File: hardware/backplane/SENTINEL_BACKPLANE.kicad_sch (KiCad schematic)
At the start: 57 parts, among them J1 SLOT1, J10 50V IN, J11 DRAIN1, J12 DRAIN2, J13 DRAIN3, J14 DRAIN4, J15 DRAIN5, J16 DRAIN6, J17 DRAIN7, J18 DRAIN8, J19 12V IN, J2 SLOT2, J3 SLOT3, J4 SLOT4, J5 SLOT5, J6 SLOT6, J7 SLOT7, J8 SLOT8, J9 TO TILE

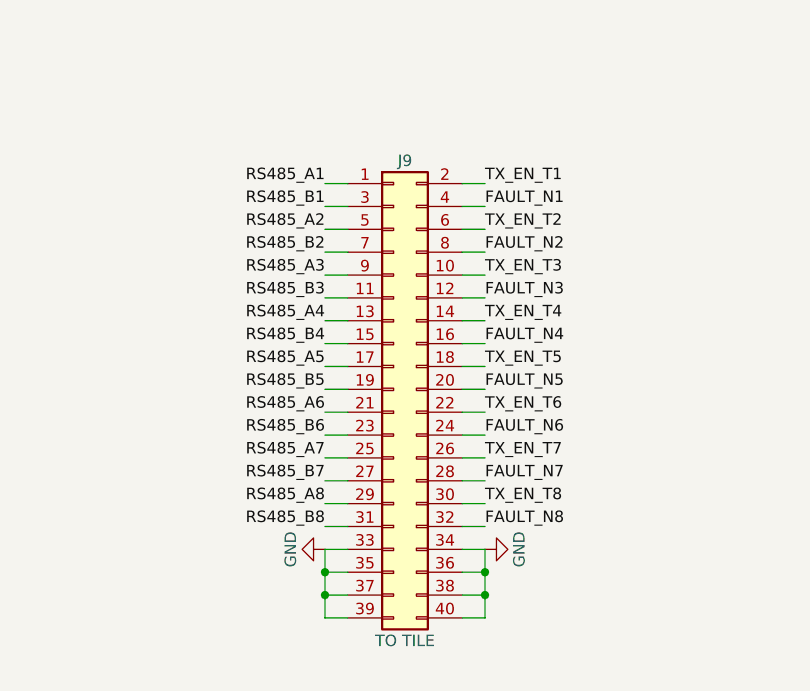
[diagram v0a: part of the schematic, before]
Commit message: Five boards DRC-clean, BOMs, layout engine improvements
- Backplane, clock & timing, calibration network, PSU and feed board layouts now pass
  KiCad DRC with zero errors and zero unconnected items
- T/R module: 0 DRC errors, 6 connections left to route by hand
- Calibration selector redesigned as an SPDT tree (replaces the fine-pitch SP8T)
- PSU: IPC-2221 2.5 mm high-voltage clearance via KiCad custom rules
- Backplane/tile cable re-pinned (slots 1-4 left column, 5-8 right) for routability
- Grouped BOM CSV for every board (hardware/tools/export_bom.sh)
- Router: partial routing, neck-downs at fine-pitch pins, long-axis fan-out,
  NPTH obstacles, pour-net connectivity, domain-aware clearance, rip-up tuning

Co-Authored-By: Claude Opus 5.5 <noreply@anthropic.com>
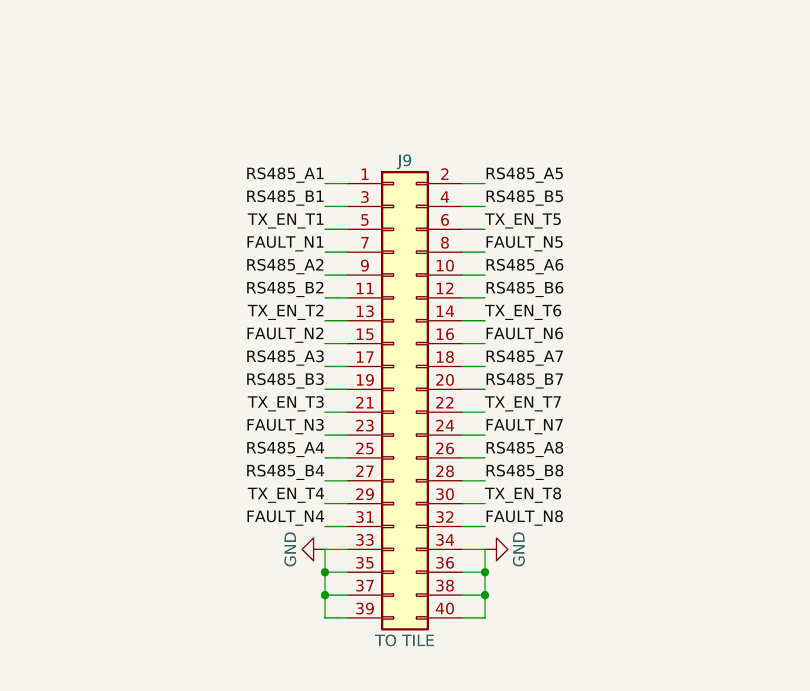
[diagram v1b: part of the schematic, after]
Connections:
- net FAULT_N1: now also J9.7 (Pin_7); no longer J9.4 (Pin_4)
- net FAULT_N2: now also J9.15 (Pin_15); no longer J9.8 (Pin_8)
- net FAULT_N3: now also J9.23 (Pin_23); no longer J9.12 (Pin_12)
- net FAULT_N4: now also J9.31 (Pin_31); no longer J9.16 (Pin_16)
- net FAULT_N5: now also J9.8 (Pin_8); no longer J9.20 (Pin_20)
- net FAULT_N6: now also J9.16 (Pin_16); no longer J9.24 (Pin_24)
- net FAULT_N7: now also J9.24 (Pin_24); no longer J9.28 (Pin_28)
- net RS485_A2: now also J9.9 (Pin_9); no longer J9.5 (Pin_5)
- net RS485_A3: now also J9.17 (Pin_17); no longer J9.9 (Pin_9)
- net RS485_A4: now also J9.25 (Pin_25); no longer J9.13 (Pin_13)
- net RS485_A5: now also J9.2 (Pin_2); no longer J9.17 (Pin_17)
- net RS485_A6: now also J9.10 (Pin_10); no longer J9.21 (Pin_21)
- net RS485_A7: now also J9.18 (Pin_18); no longer J9.25 (Pin_25)
- net RS485_A8: now also J9.26 (Pin_26); no longer J9.29 (Pin_29)
- net RS485_B2: now also J9.11 (Pin_11); no longer J9.7 (Pin_7)
- net RS485_B3: now also J9.19 (Pin_19); no longer J9.11 (Pin_11)
- net RS485_B4: now also J9.27 (Pin_27); no longer J9.15 (Pin_15)
- net RS485_B5: now also J9.4 (Pin_4); no longer J9.19 (Pin_19)
- net RS485_B6: now also J9.12 (Pin_12); no longer J9.23 (Pin_23)
- net RS485_B7: now also J9.20 (Pin_20); no longer J9.27 (Pin_27)
- net RS485_B8: now also J9.28 (Pin_28); no longer J9.31 (Pin_31)
- net TX_EN_T1: now also J9.5 (Pin_5); no longer J9.2 (Pin_2)
- net TX_EN_T2: now also J9.13 (Pin_13); no longer J9.6 (Pin_6)
- net TX_EN_T3: now also J9.21 (Pin_21); no longer J9.10 (Pin_10)
- net TX_EN_T4: now also J9.29 (Pin_29); no longer J9.14 (Pin_14)
- net TX_EN_T5: now also J9.6 (Pin_6); no longer J9.18 (Pin_18)
- net TX_EN_T6: now also J9.14 (Pin_14); no longer J9.22 (Pin_22)
- net TX_EN_T7: now also J9.22 (Pin_22); no longer J9.26 (Pin_26)
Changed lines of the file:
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@@
 		)
 	)
-	(label "TX_EN_T1"
+	(label "RS485_A5"
 		(at 289.56 193.04 0)
 		(fields_autoplaced yes)
@@
 		)
 	)
+	(label "RS485_B5"
+		(at 289.56 195.58 0)
+		(fields_autoplaced yes)
+		(effects
+			(font
+				(size 1.27 1.27)
+			)
+			(justify left bottom)
+		)
+	)
+	(label "TX_EN_T1"
+		(at 271.78 198.12 180)
+		(fields_autoplaced yes)
+		(effects
+			(font
+				(size 1.27 1.27)
+			)
+			(justify right bottom)
+		)
+	)
+	(label "TX_EN_T5"
+		(at 289.56 198.12 0)
+		(fields_autoplaced yes)
+		(effects
+			(font
+				(size 1.27 1.27)
+			)
+			(justify left bottom)
+		)
+	)
 	(label "FAULT_N1"
-		(at 289.56 195.58 0)
+		(at 271.78 200.66 180)
+		(fields_autoplaced yes)
+		(effects
+			(font
+				(size 1.27 1.27)
+			)
+			(justify right bottom)
+		)
+	)
+	(label "FAULT_N5"
+		(at 289.56 200.66 0)
 		(fields_autoplaced yes)
 		(effects
@@
 	)
 	(label "RS485_A2"
-		(at 271.78 198.12 180)
-		(fields_autoplaced yes)
-		(effects
-			(font
-				(size 1.27 1.27)
-			)
-			(justify right bottom)
+		(at 271.78 203.2 180)
+		(fields_autoplaced yes)
+		(effects
+			(font
+				(size 1.27 1.27)
+			)
+			(justify right bottom)
+		)
+	)
+	(label "RS485_A6"
+		(at 289.56 203.2 0)
+		(fields_autoplaced yes)
+		(effects
+			(font
+				(size 1.27 1.27)
+			)
+			(justify left bottom)
+		)
+	)
+	(label "RS485_B2"
+		(at 271.78 205.74 180)
+		(fields_autoplaced yes)
+		(effects
+			(font
+				(size 1.27 1.27)
+			)
+			(justify right bottom)
+		)
+	)
+	(label "RS485_B6"
+		(at 289.56 205.74 0)
+		(fields_autoplaced yes)
+		(effects
+			(font
+				(size 1.27 1.27)
+			)
+			(justify left bottom)
 		)
 	)
 	(label "TX_EN_T2"
-		(at 289.56 198.12 0)
-		(fields_autoplaced yes)
-		(effects
-			(font
-				(size 1.27 1.27)
-			)
-			(justify left bottom)
-		)
-	)
-	(label "RS485_B2"
-		(at 271.78 200.66 180)
-		(fields_autoplaced yes)
-		(effects
-			(font
-				(size 1.27 1.27)
-			)
-			(justify right bottom)
+		(at 271.78 208.28 180)
+		(fields_autoplaced yes)
+		(effects
+			(font
+				(size 1.27 1.27)
+			)
+			(justify right bottom)
+		)
+	)
+	(label "TX_EN_T6"
+		(at 289.56 208.28 0)
+		(fields_autoplaced yes)
+		(effects
+			(font
+				(size 1.27 1.27)
+			)
+			(justify left bottom)
 		)
 	)
 	(label "FAULT_N2"
-		(at 289.56 200.66 0)
+		(at 271.78 210.82 180)
+		(fields_autoplaced yes)
+		(effects
+			(font
+				(size 1.27 1.27)
+			)
+			(justify right bottom)
+		)
+	)
+	(label "FAULT_N6"
+		(at 289.56 210.82 0)
 		(fields_autoplaced yes)
 		(effects
@@
 	)
 	(label "RS485_A3"
-		(at 271.78 203.2 180)
-		(fields_autoplaced yes)
-		(effects
-			(font
-				(size 1.27 1.27)
-			)
-			(justify right bottom)
+		(at 271.78 213.36 180)
+		(fields_autoplaced yes)
+		(effects
+			(font
+				(size 1.27 1.27)
+			)
+			(justify right bottom)
+		)
+	)
+	(label "RS485_A7"
+		(at 289.56 213.36 0)
+		(fields_autoplaced yes)
+		(effects
+			(font
+				(size 1.27 1.27)
+			)
+			(justify left bottom)
+		)
+	)
+	(label "RS485_B3"
+		(at 271.78 215.9 180)
+		(fields_autoplaced yes)
+		(effects
+			(font
+				(size 1.27 1.27)
+			)
+			(justify right bottom)
+		)
+	)
+	(label "RS485_B7"
+		(at 289.56 215.9 0)
+		(fields_autoplaced yes)
+		(effects
+			(font
+				(size 1.27 1.27)
+			)
+			(justify left bottom)
 		)
 	)
 	(label "TX_EN_T3"
-		(at 289.56 203.2 0)
-		(fields_autoplaced yes)
-		(effects
-			(font
-				(size 1.27 1.27)
-			)
-			(justify left bottom)
-		)
-	)
-	(label "RS485_B3"
-		(at 271.78 205.74 180)
-		(fields_autoplaced yes)
-		(effects
-			(font
-				(size 1.27 1.27)
-			)
-			(justify right bottom)
+		(at 271.78 218.44 180)
+		(fields_autoplaced yes)
+		(effects
+			(font
+				(size 1.27 1.27)
+			)
+			(justify right bottom)
+		)
+	)
+	(label "TX_EN_T7"
+		(at 289.56 218.44 0)
+		(fields_autoplaced yes)
+		(effects
+			(font
+				(size 1.27 1.27)
+			)
+			(justify left bottom)
 		)
 	)
 	(label "FAULT_N3"
-		(at 289.56 205.74 0)
+		(at 271.78 220.98 180)
+		(fields_autoplaced yes)
+		(effects
+			(font
+				(size 1.27 1.27)
+			)
+			(justify right bottom)
+		)
+	)
+	(label "FAULT_N7"
+		(at 289.56 220.98 0)
 		(fields_autoplaced yes)
 		(effects
@@
 	)
 	(label "RS485_A4"
-		(at 271.78 208.28 180)
-		(fields_autoplaced yes)
-		(effects
-			(font
-				(size 1.27 1.27)
-			)
-			(justify right bottom)
+		(at 271.78 223.52 180)
+		(fields_autoplaced yes)
+		(effects
+			(font
+				(size 1.27 1.27)
+			)
+			(justify right bottom)
+		)
+	)
+	(label "RS485_A8"
+		(at 289.56 223.52 0)
+		(fields_autoplaced yes)
+		(effects
+			(font
+				(size 1.27 1.27)
+			)
+			(justify left bottom)
+		)
+	)
+	(label "RS485_B4"
+		(at 271.78 226.06 180)
+		(fields_autoplaced yes)
+		(effects
+			(font
+				(size 1.27 1.27)
+			)
+			(justify right bottom)
+		)
+	)
+	(label "RS485_B8"
+		(at 289.56 226.06 0)
+		(fields_autoplaced yes)
+		(effects
+			(font
+				(size 1.27 1.27)
+			)
+			(justify left bottom)
 		)
 	)
 	(label "TX_EN_T4"
-		(at 289.56 208.28 0)
-		(fields_autoplaced yes)
-		(effects
-			(font
-				(size 1.27 1.27)
-			)
-			(justify left bottom)
-		)
-	)
-	(label "RS485_B4"
-		(at 271.78 210.82 180)
-		(fields_autoplaced yes)
-		(effects
-			(font
-				(size 1.27 1.27)
-			)
-			(justify right bottom)
-		)
-	)
-	(label "FAULT_N4"
-		(at 289.56 210.82 0)
-		(fields_autoplaced yes)
-		(effects
-			(font
-				(size 1.27 1.27)
-			)
-			(justify left bottom)
-		)
-	)
-	(label "RS485_A5"
-		(at 271.78 213.36 180)
-		(fields_autoplaced yes)
-		(effects
-			(font
-				(size 1.27 1.27)
-			)
-			(justify right bottom)
-		)
-	)
-	(label "TX_EN_T5"
-		(at 289.56 213.36 0)
-		(fields_autoplaced yes)
-		(effects
-			(font
-				(size 1.27 1.27)
-			)
-			(justify left bottom)
-		)
-	)
-	(label "RS485_B5"
-		(at 271.78 215.9 180)
-		(fields_autoplaced yes)
-		(effects
-			(font
-				(size 1.27 1.27)
-			)
-			(justify right bottom)
-		)
-	)
-	(label "FAULT_N5"
-		(at 289.56 215.9 0)
-		(fields_autoplaced yes)
-		(effects
-			(font
-				(size 1.27 1.27)
-			)
-			(justify left bottom)
-		)
-	)
-	(label "RS485_A6"
-		(at 271.78 218.44 180)
-		(fields_autoplaced yes)
-		(effects
-			(font
-				(size 1.27 1.27)
-			)
-			(justify right bottom)
-		)
-	)
-	(label "TX_EN_T6"
-		(at 289.56 218.44 0)
-		(fields_autoplaced yes)
-		(effects
-			(font
-				(size 1.27 1.27)
-			)
-			(justify left bottom)
-		)
-	)
-	(label "RS485_B6"
-		(at 271.78 220.98 180)
-		(fields_autoplaced yes)
-		(effects
-			(font
-				(size 1.27 1.27)
-			)
-			(justify right bottom)
-		)
-	)
-	(label "FAULT_N6"
-		(at 289.56 220.98 0)
-		(fields_autoplaced yes)
-		(effects
-			(font
-				(size 1.27 1.27)
-			)
-			(justify left bottom)
-		)
-	)
-	(label "RS485_A7"
-		(at 271.78 223.52 180)
-		(fields_autoplaced yes)
-		(effects
-			(font
-				(size 1.27 1.27)
-			)
-			(justify right bottom)
-		)
-	)
-	(label "TX_EN_T7"
-		(at 289.56 223.52 0)
-		(fields_autoplaced yes)
-		(effects
-			(font
-				(size 1.27 1.27)
-			)
-			(justify left bottom)
-		)
-	)
-	(label "RS485_B7"
-		(at 271.78 226.06 180)
-		(fields_autoplaced yes)
-		(effects
-			(font
-				(size 1.27 1.27)
-			)
-			(justify right bottom)
-		)
-	)
-	(label "FAULT_N7"
-		(at 289.56 226.06 0)
-		(fields_autoplaced yes)
-		(effects
-			(font
-				(size 1.27 1.27)
-			)
-			(justify left bottom)
-		)
-	)
-	(label "RS485_A8"
 		(at 271.78 228.6 180)
 		(fields_autoplaced yes)
@@
 		)
 	)
-	(label "RS485_B8"
+	(label "FAULT_N4"
 		(at 271.78 231.14 180)
 		(fields_autoplaced yes)
